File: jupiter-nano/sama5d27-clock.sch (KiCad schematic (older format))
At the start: 14 parts, among them U1 ATSAMA5D27C-LD1G-CU, Y1 NX2012SA-32.768KHZ-EXS00A-MU0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, Y2 NX3225SA-12MHZ-STD-CSR-3

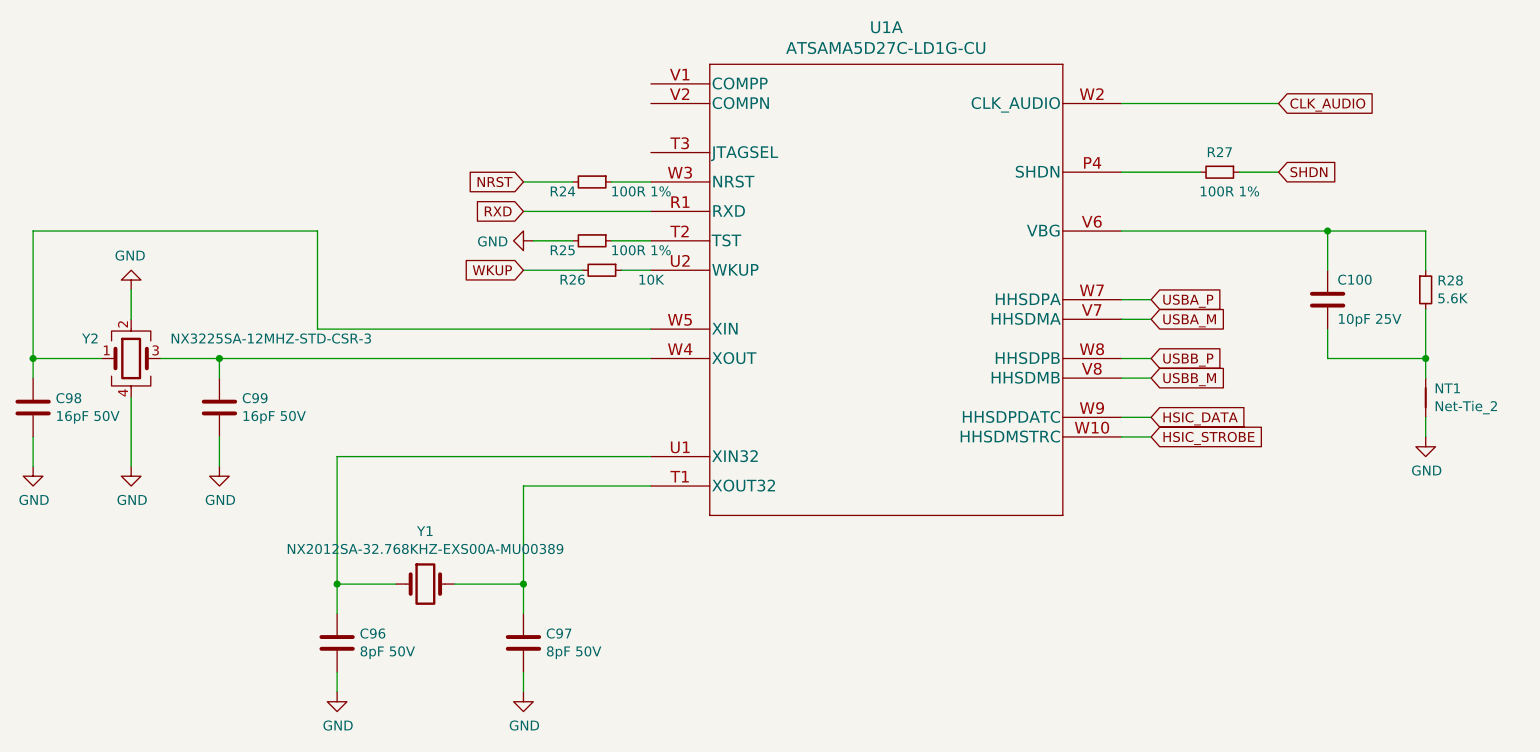
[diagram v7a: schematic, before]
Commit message: numerous ERC fixes
- still more to go
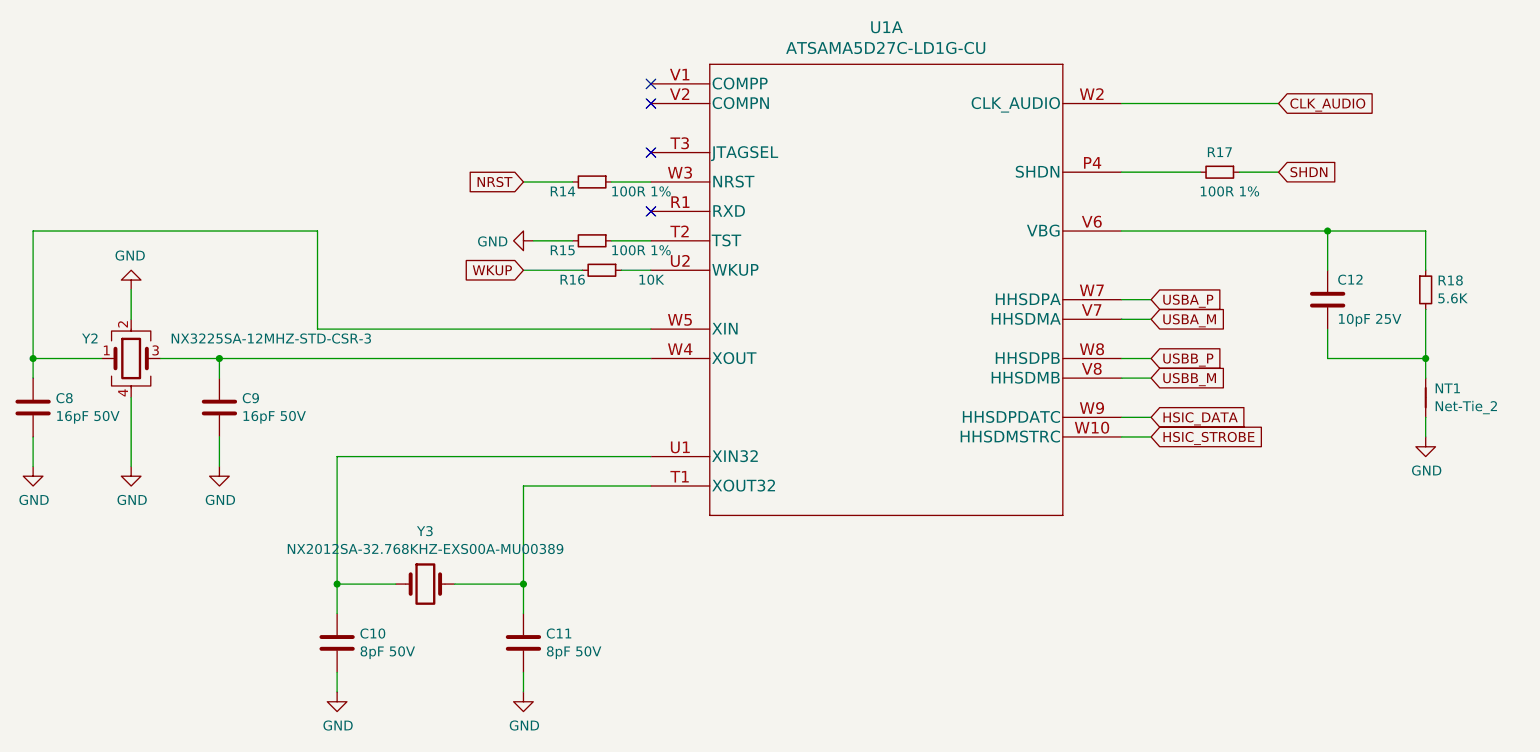
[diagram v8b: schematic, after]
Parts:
- renumbered C96 to C10, C97 to C11, C100 to C12, C98 to C8, C99 to C9, R24 to R14, R25 to R15, R26 to R16, R27 to R17, R28 to R18, Y1 to Y3
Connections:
- net RXD: no longer names the net of U1.R1 (RXD)
- no-connect marks 0 -> 4
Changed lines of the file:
@@
 $EndComp
 $Comp
-L Device:C C98
+L Device:C C8
 U 1 1 5FB8C3A7
 P 1300 3900
-F 0 "C98" H 1415 3946 50  0000 L CNN
+F 0 "C8" H 1415 3946 50  0000 L CNN
 F 1 "16pF 50V" H 1415 3855 50  0000 L CNN
 F 2 "" H 1338 3750 50  0001 C CNN
@@
 $EndComp
 $Comp
-L Device:C C99
+L Device:C C9
 U 1 1 5FB8D41E
 P 2250 3900
-F 0 "C99" H 2365 3946 50  0000 L CNN
+F 0 "C9" H 2365 3946 50  0000 L CNN
 F 1 "16pF 50V" H 2365 3855 50  0000 L CNN
 F 2 "" H 2288 3750 50  0001 C CNN
@@
 $EndComp
 $Comp
-L Device:C C96
+L Device:C C10
 U 1 1 5FB8E15B
 P 2850 5100
-F 0 "C96" H 2965 5146 50  0000 L CNN
+F 0 "C10" H 2965 5146 50  0000 L CNN
 F 1 "8pF 50V" H 2965 5055 50  0000 L CNN
 F 2 "" H 2888 4950 50  0001 C CNN
@@
 $EndComp
 $Comp
-L Device:C C100
+L Device:C C12
 U 1 1 5FB8E9C8
 P 7900 3350
-F 0 "C100" H 7950 3450 50  0000 L CNN
+F 0 "C12" H 7950 3450 50  0000 L CNN
 F 1 "10pF 25V" H 7950 3250 50  0000 L CNN
 F 2 "" H 7938 3200 50  0001 C CNN
@@
 $EndComp
 $Comp
-L Device:R_Small R24
+L Device:R_Small R14
 U 1 1 5FB9019B
 P 4150 2750
-F 0 "R24" V 4200 2600 50  0000 C CNN
+F 0 "R14" V 4200 2600 50  0000 C CNN
 F 1 "100R 1%" V 4200 3000 50  0000 C CNN
 F 2 "" H 4150 2750 50  0001 C CNN
@@
 $EndComp
 $Comp
-L Device:R_Small R26
+L Device:R_Small R16
 U 1 1 5FB90BC4
 P 4200 3200
-F 0 "R26" V 4250 3050 50  0000 C CNN
+F 0 "R16" V 4250 3050 50  0000 C CNN
 F 1 "10K" V 4250 3450 50  0000 C CNN
 F 2 "" H 4200 3200 50  0001 C CNN
@@
 $EndComp
 $Comp
-L Device:R_Small R27
+L Device:R_Small R17
 U 1 1 5FB913F4
 P 7350 2700
-F 0 "R27" V 7250 2700 50  0000 C CNN
+F 0 "R17" V 7250 2700 50  0000 C CNN
 F 1 "100R 1%" V 7450 2750 50  0000 C CNN
 F 2 "" H 7350 2700 50  0001 C CNN
@@
 $EndComp
 $Comp
-L Device:R_Small R25
+L Device:R_Small R15
 U 1 1 5FB91AFA
 P 4150 3050
-F 0 "R25" V 4200 2900 50  0000 C CNN
+F 0 "R15" V 4200 2900 50  0000 C CNN
 F 1 "100R 1%" V 4200 3300 50  0000 C CNN
 F 2 "" H 4150 3050 50  0001 C CNN
@@
 	3850 3050 4050 3050
 $Comp
-L power:GND #PWR0124
+L power:GND #PWR031
 U 1 1 5FBB7C84
 P 3850 3050
-F 0 "#PWR0124" H 3850 2800 50  0001 C CNN
+F 0 "#PWR031" H 3850 2800 50  0001 C CNN
 F 1 "GND" V 3855 2922 50  0000 R CNN
 F 2 "" H 3850 3050 50  0001 C CNN
@@
 $EndComp
 Wire Wire Line
-	4450 2900 3800 2900
-Text GLabel 3800 2900 0    50   Input ~ 0
-RXD
-Wire Wire Line
 	6850 2350 7650 2350
 Text GLabel 7650 2350 2    50   Input ~ 0
@@
 Connection ~ 8400 3650
 $Comp
-L power:GND #PWR0125
+L power:GND #PWR032
 U 1 1 5FBD26A3
 P 8400 4050
-F 0 "#PWR0125" H 8400 3800 50  0001 C CNN
+F 0 "#PWR032" H 8400 3800 50  0001 C CNN
 F 1 "GND" H 8405 3877 50  0000 C CNN
 F 2 "" H 8400 4050 50  0001 C CNN
@@
 HSIC_STROBE
 $Comp
-L Device:Crystal Y1
+L Device:Crystal Y3
 U 1 1 5FE530E7
 P 3300 4800
-F 0 "Y1" H 3300 5068 50  0000 C CNN
+F 0 "Y3" H 3300 5068 50  0000 C CNN
 F 1 "NX2012SA-32.768KHZ-EXS00A-MU00389" H 3300 4977 50  0000 C CNN
 F 2 "" H 3300 4800 50  0001 C CNN
@@
 	2250 4050 2250 4200
 $Comp
-L power:GND #PWR0126
+L power:GND #PWR025
 U 1 1 5FE58F04
 P 1300 4200
-F 0 "#PWR0126" H 1300 3950 50  0001 C CNN
+F 0 "#PWR025" H 1300 3950 50  0001 C CNN
 F 1 "GND" H 1305 4027 50  0000 C CNN
 F 2 "" H 1300 4200 50  0001 C CNN
@@
 $EndComp
 $Comp
-L power:GND #PWR0127
+L power:GND #PWR027
 U 1 1 5FE592EB
 P 1800 4200
-F 0 "#PWR0127" H 1800 3950 50  0001 C CNN
+F 0 "#PWR027" H 1800 3950 50  0001 C CNN
 F 1 "GND" H 1805 4027 50  0000 C CNN
 F 2 "" H 1800 4200 50  0001 C CNN
@@
 $EndComp
 $Comp
-L power:GND #PWR0128
+L power:GND #PWR028
 U 1 1 5FE59993
 P 2250 4200
-F 0 "#PWR0128" H 2250 3950 50  0001 C CNN
+F 0 "#PWR028" H 2250 3950 50  0001 C CNN
 F 1 "GND" H 2255 4027 50  0000 C CNN
 F 2 "" H 2250 4200 50  0001 C CNN
@@
 	1800 3450 1800 3300
 $Comp
-L power:GND #PWR0129
+L power:GND #PWR026
 U 1 1 5FE62514
 P 1800 3300
-F 0 "#PWR0129" H 1800 3050 50  0001 C CNN
+F 0 "#PWR026" H 1800 3050 50  0001 C CNN
 F 1 "GND" H 1805 3127 50  0000 C CNN
 F 2 "" H 1800 3300 50  0001 C CNN
@@
 	3800 4800 3450 4800
 $Comp
-L Device:C C97
+L Device:C C11
 U 1 1 5FE68FD7
 P 3800 5100
-F 0 "C97" H 3915 5146 50  0000 L CNN
+F 0 "C11" H 3915 5146 50  0000 L CNN
 F 1 "8pF 50V" H 3915 5055 50  0000 L CNN
 F 2 "" H 3838 4950 50  0001 C CNN
@@
 Connection ~ 3800 4800
 $Comp
-L power:GND #PWR0130
+L power:GND #PWR029
 U 1 1 5FE6D6B8
 P 2850 5350
-F 0 "#PWR0130" H 2850 5100 50  0001 C CNN
+F 0 "#PWR029" H 2850 5100 50  0001 C CNN
 F 1 "GND" H 2855 5177 50  0000 C CNN
 F 2 "" H 2850 5350 50  0001 C CNN
@@
 $EndComp
 $Comp
-L power:GND #PWR0131
+L power:GND #PWR030
 U 1 1 5FE6DCB8
 P 3800 5350
-F 0 "#PWR0131" H 3800 5100 50  0001 C CNN
+F 0 "#PWR030" H 3800 5100 50  0001 C CNN
 F 1 "GND" H 3805 5177 50  0000 C CNN
 F 2 "" H 3800 5350 50  0001 C CNN
@@
 	8400 3950 8400 4050
 $Comp
-L Device:R_Small R28
+L Device:R_Small R18
 U 1 1 5FB8F66D
 P 8400 3300
-F 0 "R28" H 8459 3346 50  0000 L CNN
+F 0 "R18" H 8459 3346 50  0000 L CNN
 F 1 "5.6K" H 8459 3255 50  0000 L CNN
 F 2 "" H 8400 3300 50  0001 C CNN
@@
 	1    0    0    -1
 $EndComp
+NoConn ~ 4450 2250
+NoConn ~ 4450 2350
+NoConn ~ 4450 2600
+NoConn ~ 4450 2900
 $EndSCHEMATC
